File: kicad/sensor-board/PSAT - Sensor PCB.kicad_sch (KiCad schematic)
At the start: 57 parts, among them J1 5015680407, J3 Conn_01x03_Pin, J4 5015680407 (X3), J5 5015680407, J6 MCU - Conn_01x04, Q1 2N2222A, U2 ADXL345, U3 ADXL375, U4 CD-PA1616D, U5 ESP32-CAM, U6 BME280

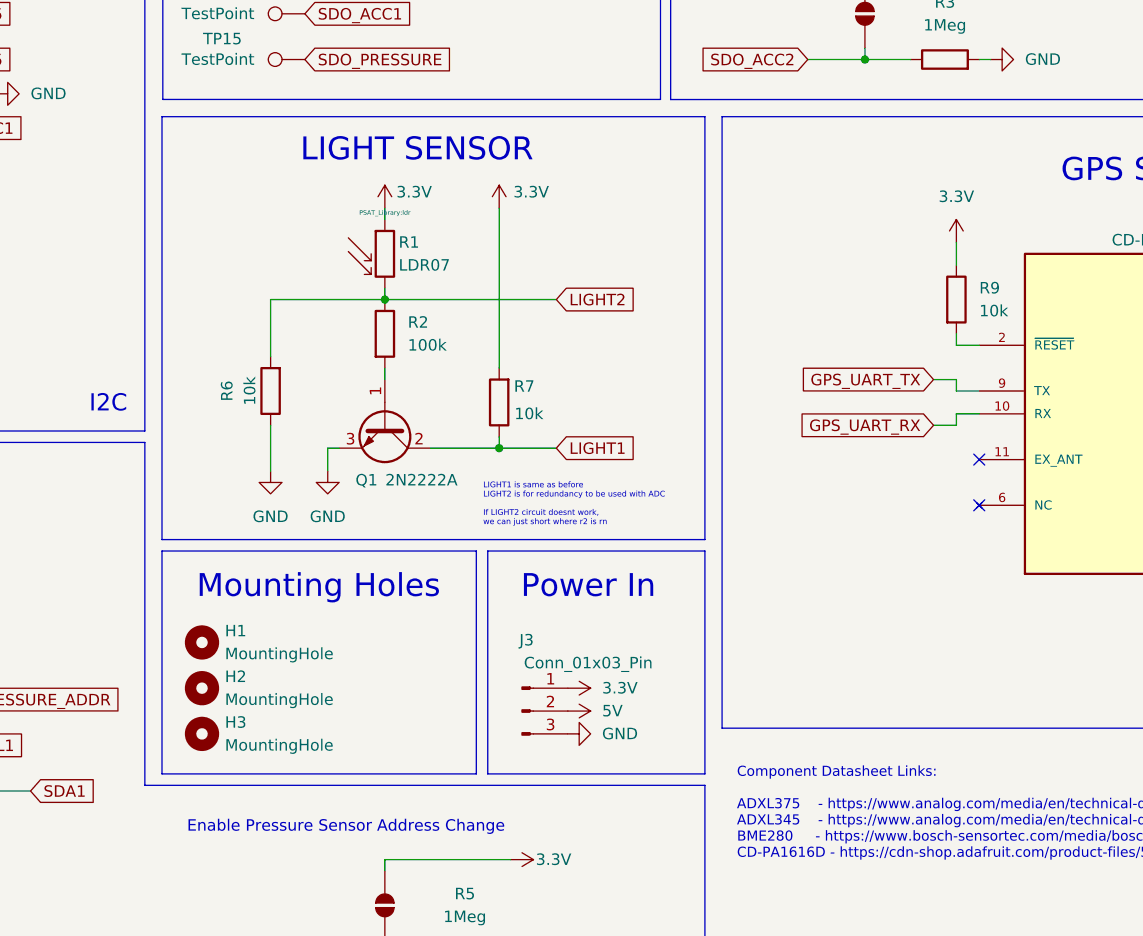
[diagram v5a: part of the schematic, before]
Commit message: feat: Completed sensor board
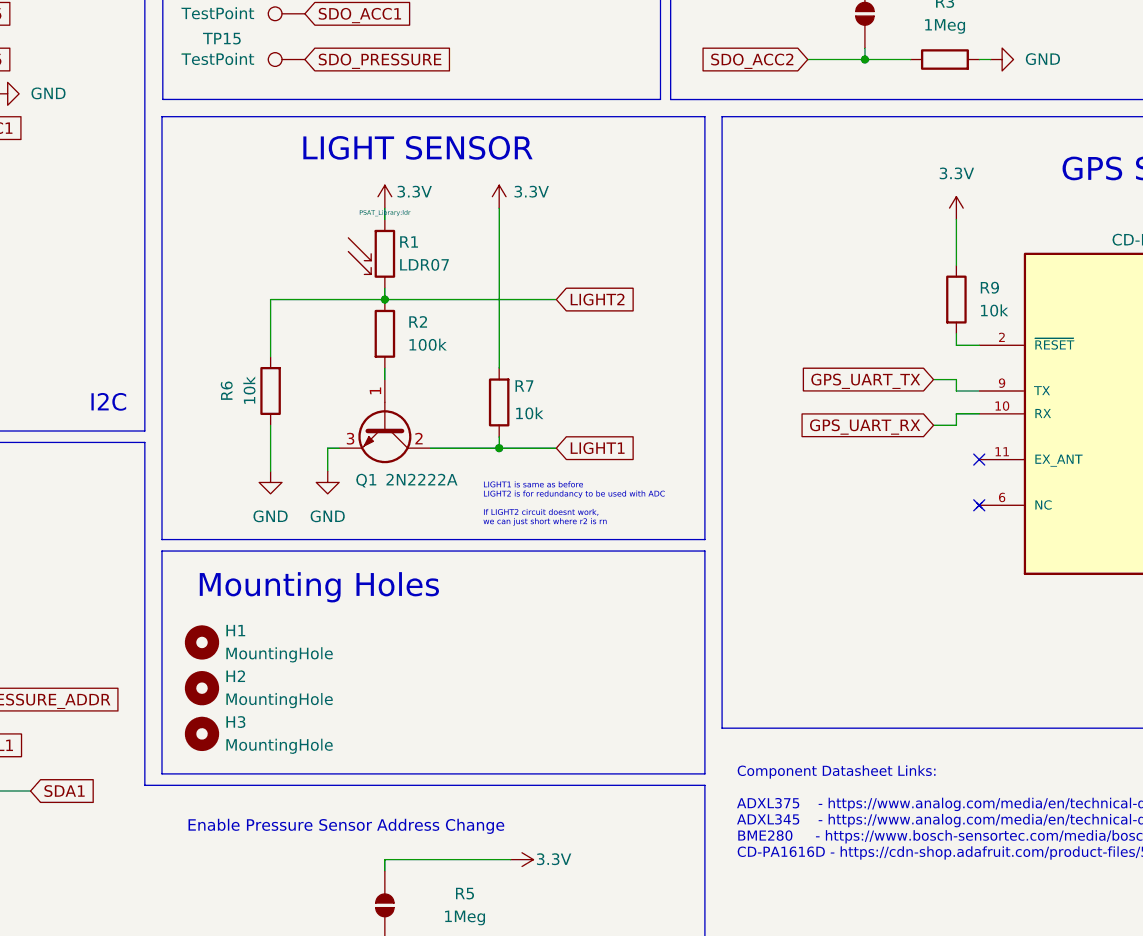
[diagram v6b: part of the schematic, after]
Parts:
- removed J3: Conn_01x03_Pin, Connector_PinHeader_2.54mm:PinHeader_1x03_P2.54mm_Vertical, symbol Connector:Conn_01x03_Pin
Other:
- note removed: "Power In"

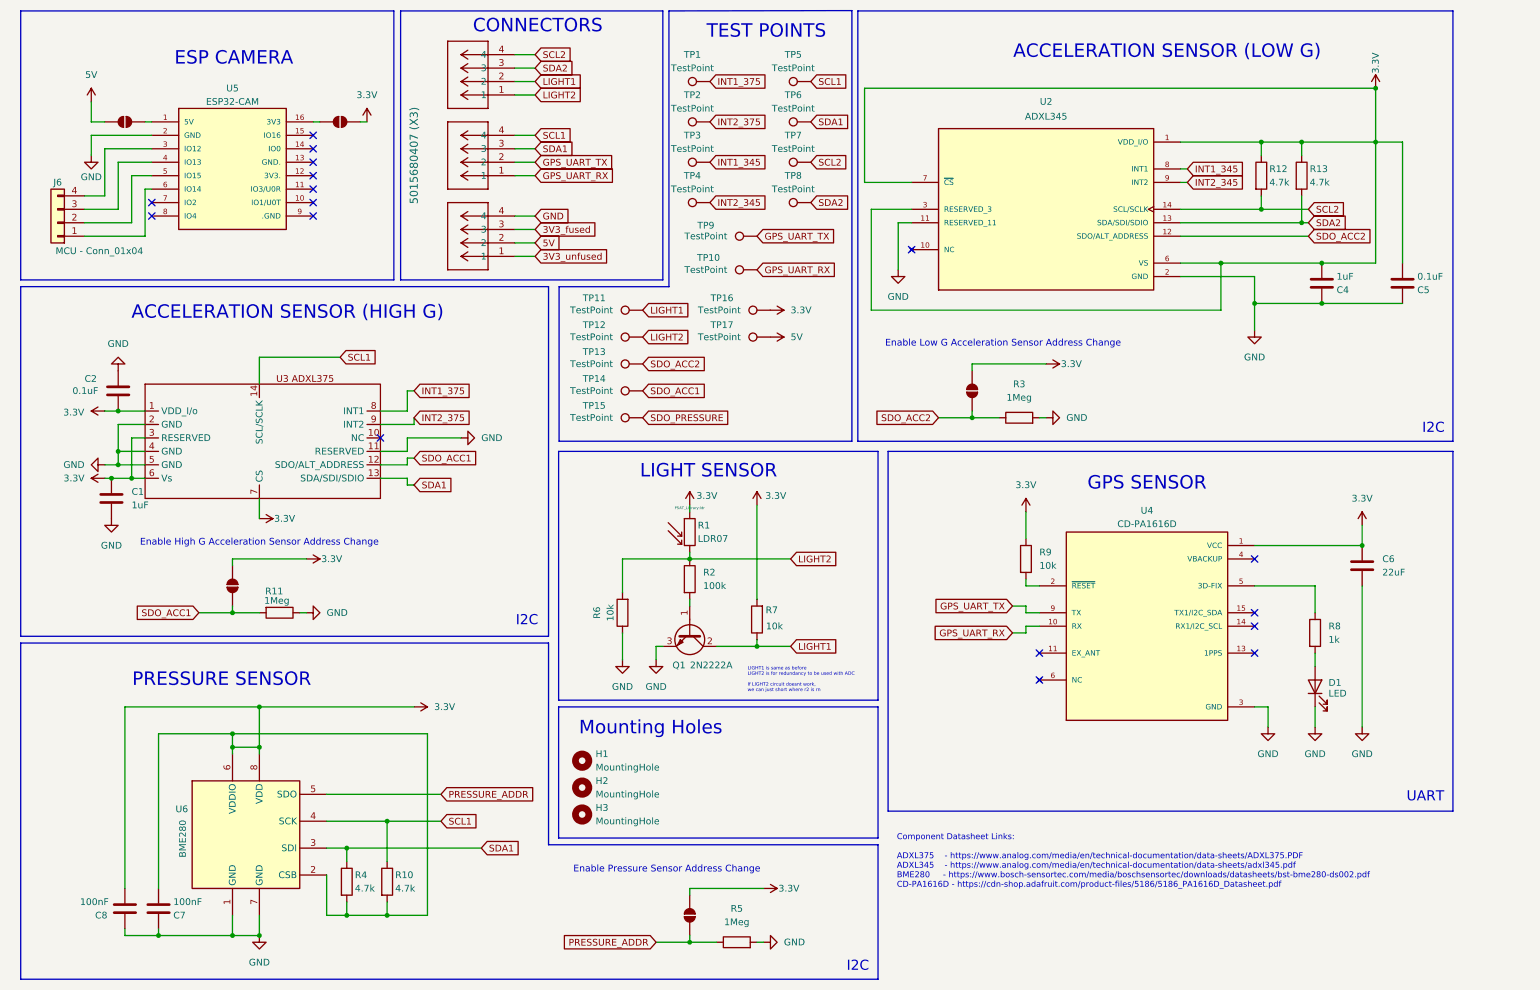
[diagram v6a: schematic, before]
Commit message: feat: Changed labels & started pcb wiring
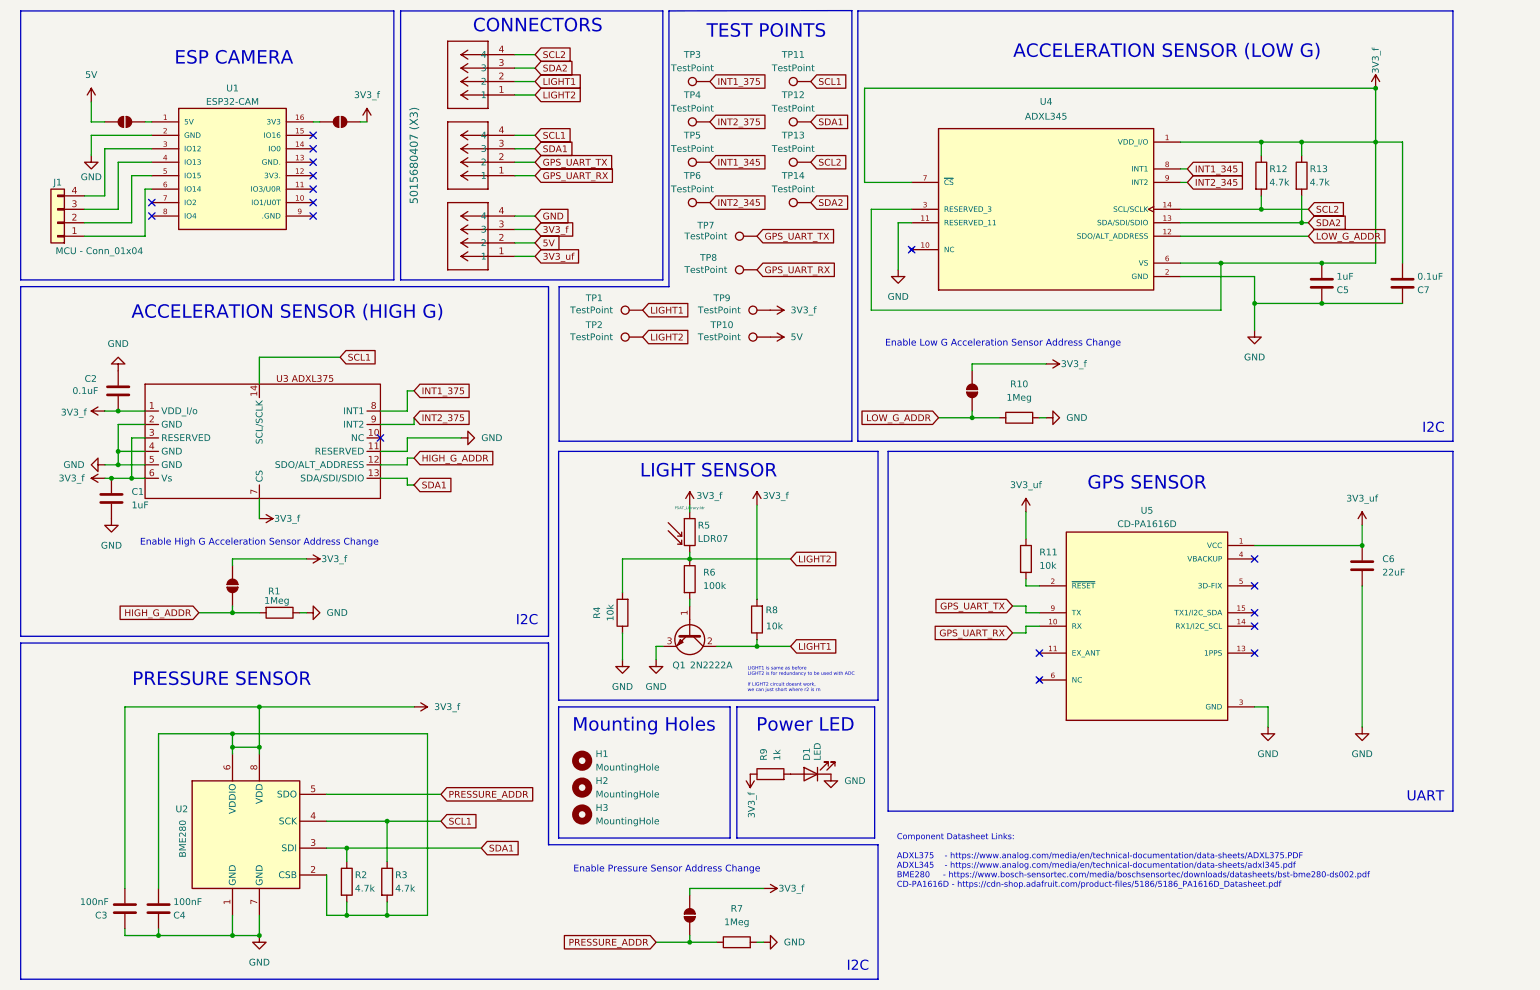
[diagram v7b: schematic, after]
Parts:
- removed TP13, TP14, TP15: TestPoint, symbol Connector:TestPoint
- TP1: renamed from TP11; footprint (none) -> TestPoint:TestPoint_Pad_D1.0mm
- TP10: renamed from TP17; footprint (none) -> TestPoint:TestPoint_Pad_D1.0mm
- TP11: renamed from TP5; footprint (none) -> TestPoint:TestPoint_Pad_D1.0mm
- TP12: renamed from TP6; footprint (none) -> TestPoint:TestPoint_Pad_D1.0mm
- TP13: renamed from TP7; footprint (none) -> TestPoint:TestPoint_Pad_D1.0mm
- TP14: renamed from TP8; footprint (none) -> TestPoint:TestPoint_Pad_D1.0mm
- TP2: renamed from TP12; footprint (none) -> TestPoint:TestPoint_Pad_D1.0mm
- TP3: renamed from TP1; footprint (none) -> TestPoint:TestPoint_Pad_D1.0mm
- TP4: renamed from TP2; footprint (none) -> TestPoint:TestPoint_Pad_D1.0mm
- TP5: renamed from TP3; footprint (none) -> TestPoint:TestPoint_Pad_D1.0mm
- TP6: renamed from TP4; footprint (none) -> TestPoint:TestPoint_Pad_D1.0mm
- TP7: renamed from TP9; footprint (none) -> TestPoint:TestPoint_Pad_D1.0mm
- TP8: renamed from TP10; footprint (none) -> TestPoint:TestPoint_Pad_D1.0mm
- TP9: renamed from TP16; footprint (none) -> TestPoint:TestPoint_Pad_D1.0mm
- renumbered C8 to C3, C7 to C4, C4 to C5, C5 to C7, J6 to J1, J5 to J2, J4 to J3, J1 to J4, JP4 to JP1, JP5 to JP4, JP1 to JP5, R11 to R1, R3 to R10, R9 to R11, R4 to R2, R10 to R3, R6 to R4, R1 to R5, R2 to R6, R5 to R7, R7 to R8, R8 to R9, U5 to U1, U6 to U2, U2 to U4, U4 to U5
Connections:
- net 3V3_fused is gone; now on net 3V3_f: J4.3
- net at U5.5 (3D-FIX): no longer R9.1
- net 3.3V renamed 3V3_f
- net 3V3_f: now also R9.1; no longer C6.1, R11.1, U5.1 (VCC)
- net 3V3_unfused renamed 3V3_uf
- net 3V3_uf: now also C6.1, R11.1, U5.1 (VCC)
- net SDO_ACC1 renamed HIGH_G_ADDR
- net SDO_ACC2 renamed LOW_G_ADDR
- no-connect marks 17 -> 18
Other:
- note added: "Power LED"
- moved on the sheet: D1, R9

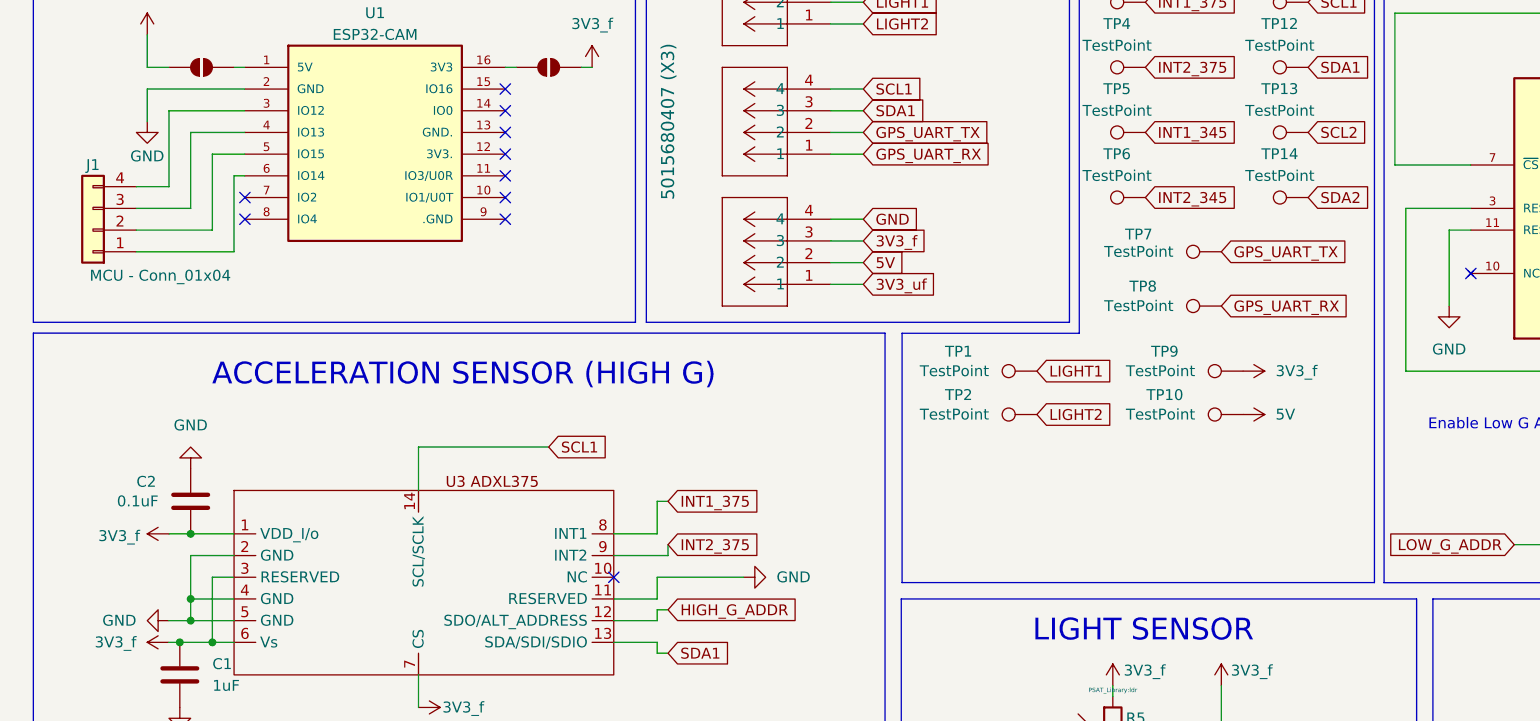
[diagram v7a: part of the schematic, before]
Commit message: feat: Changed ESP32 connectors
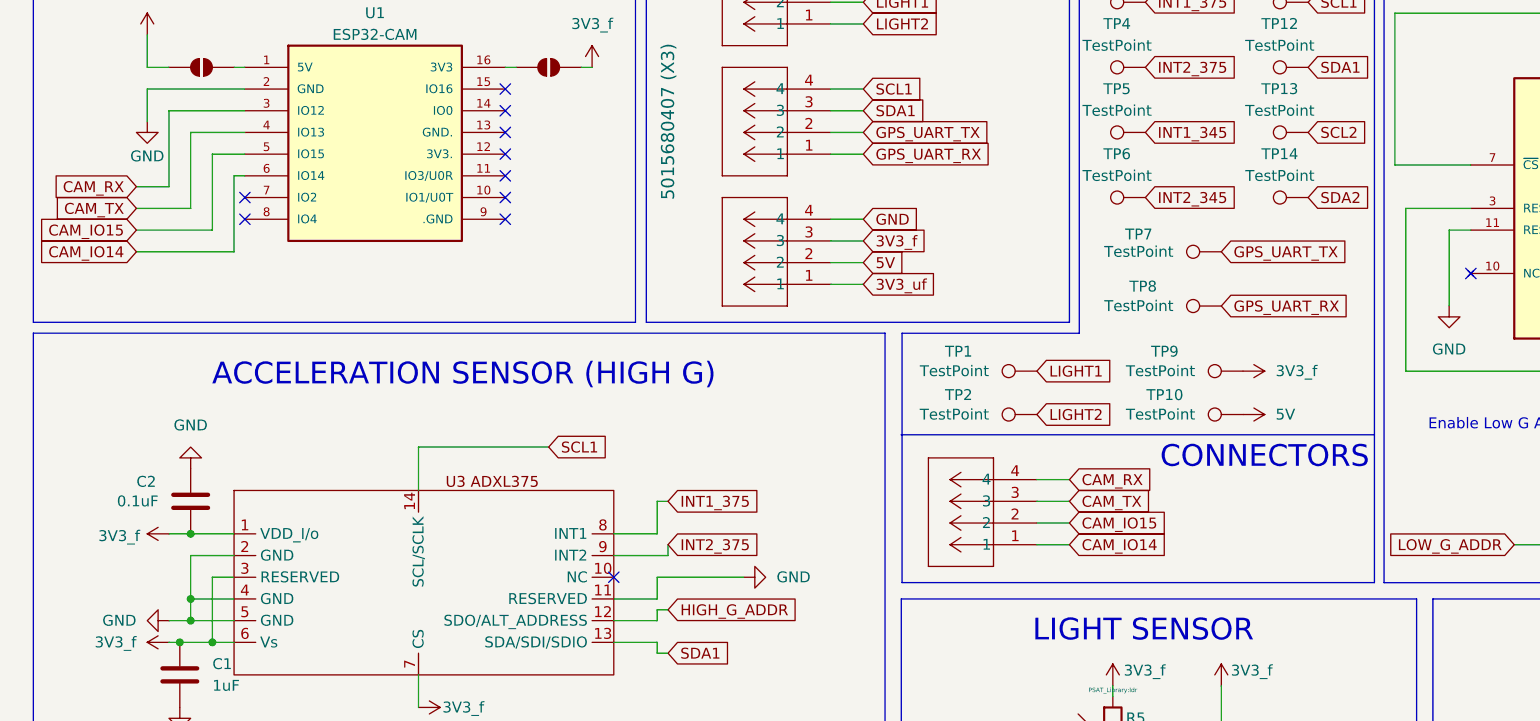
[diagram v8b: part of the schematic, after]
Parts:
- removed J1: MCU - Conn_01x04, Connector_PinHeader_2.54mm:PinHeader_1x04_P2.54mm_Vertical, symbol Connector_Generic:Conn_01x04
- added J1: 5015680407, footprints:CONN_5015680000-SD_04_MOL, symbol 2026-01-26_05-30-52:5015680407
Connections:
- net CAM_RX: now reaches U1.3 (IO12)
- net CAM_RX: now also J1.4
- net CAM_TX: now reaches U1.4 (IO13)
- net CAM_TX: now also J1.3
- net CAM_IO15: now reaches U1.5 (IO15)
- net CAM_IO15: now also J1.2
- net CAM_IO14: now reaches U1.6 (IO14)
- net CAM_IO14: now also J1.1
